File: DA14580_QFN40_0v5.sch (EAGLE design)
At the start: 29 parts, among them CON1 CON_TC2030-CTL-NL, IC1 IC_MEMORY_8P_AT25XE011_SOP, IC2 NC7SZ00M5XCT-ND, IC3 LDO5_3.3_SOT23, Q1 728-1076-1-ND, Q2 16M_2520, U1 DA14583AT2, X1 SSW-114-02-S-S, X2 SSW-114-02-S-S

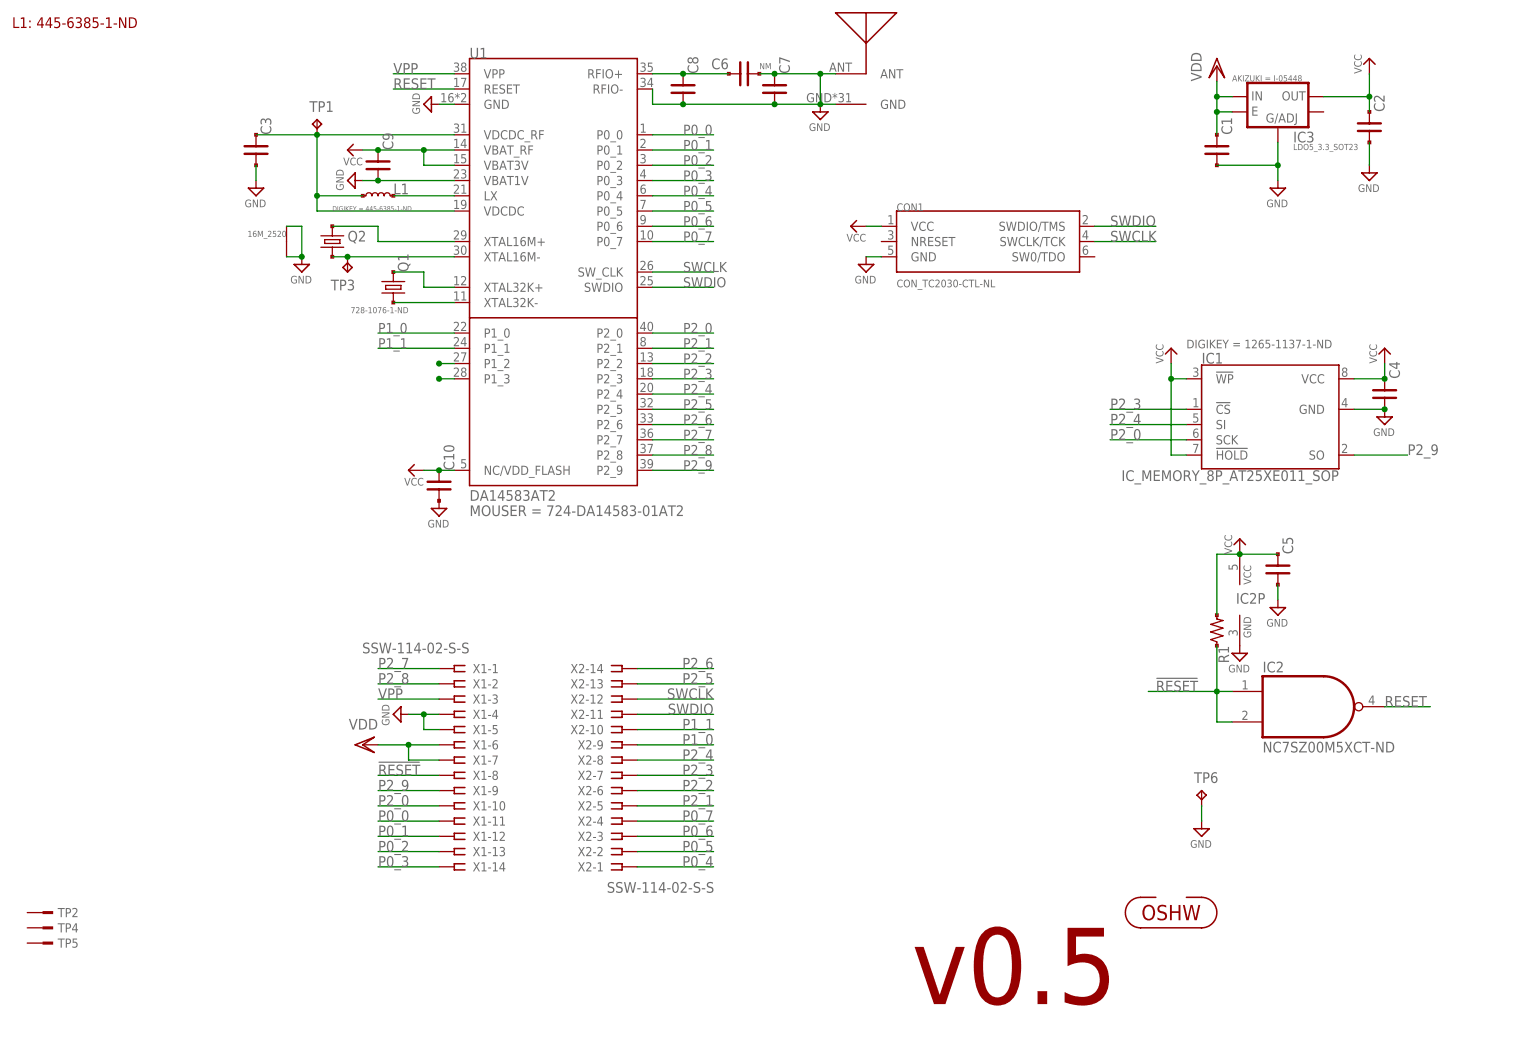
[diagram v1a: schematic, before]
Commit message: [ 58x ] IC1 - tCream; add a selecter (580 or 583)
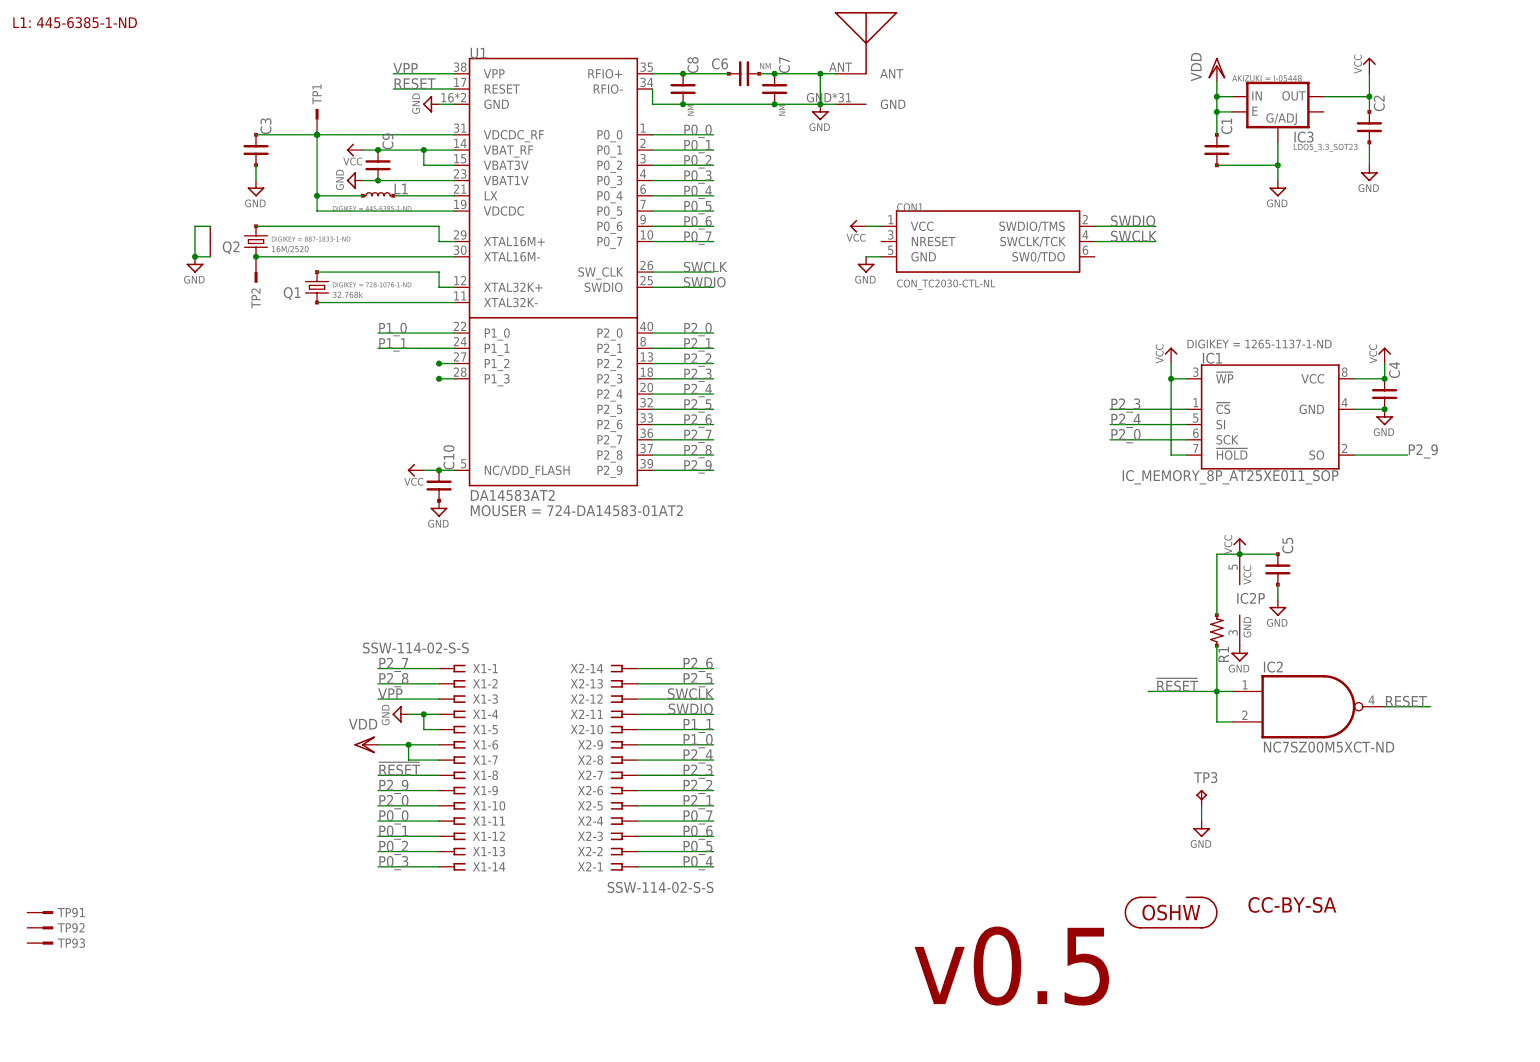
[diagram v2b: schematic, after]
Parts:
- removed TP6: TPPAD1-13, testpad_local:TPPAD1-13
- added TP91: TESTPAD_F, mylib:TESTPAD_F
- C7, C8: value (none) -> NM
- Q1: value 728-1076-1-ND -> 32.768k
- Q2: value 16M_2520 -> 16M/2520
- TP1: value TPTP07R -> TESTPAD; device testpad_local:TPTP07R -> mylib:TESTPAD
- TP2: value TESTPAD_F -> TESTPAD; device mylib:TESTPAD_F -> mylib:TESTPAD
- TP3: value TPTP07R -> TPPAD1-13; device testpad_local:TPTP07R -> testpad_local:TPPAD1-13
- renumbered TP4 to TP92, TP5 to TP93
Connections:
- net GND: now also TP3.TP; no longer TP6.TP
- net N$21: now also TP2.1; no longer TP3.TP
- net N$9: now also TP1.1; no longer TP1.TP
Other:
- note added: "CC-BY-SA"
- moved on the sheet: Q1, Q2, TP2, TP3
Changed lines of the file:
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@@
 <part name="VDD1" library="supply1" deviceset="VDD" device=""/>
 <part name="P+1" library="mylib" deviceset="VCC" device=""/>
-<part name="Q1" library="mylib" deviceset="CRYSTAL2_*" device="_FC-135" technology="32.768K" value="728-1076-1-ND"/>
+<part name="Q1" library="mylib" deviceset="CRYSTAL2_*" device="_FC-135" technology="32.768K" value="32.768k"/>
 <part name="SUPPLY7" library="mylib" deviceset="GND" device=""/>
 <part name="SUPPLY8" library="mylib" deviceset="GND" device=""/>
@@
 <part name="C4" library="mylib" deviceset="C_SMD_*" device="_1005" technology="0.1U"/>
 <part name="SUPPLY13" library="mylib" deviceset="GND" device=""/>
-<part name="TP1" library="testpad_local" deviceset="TP" device="TP07R" value="TPTP07R"/>
 <part name="X1" library="con-samtec.local" deviceset="SSW-114-02-S-S" device=""/>
 <part name="X2" library="con-samtec.local" deviceset="SSW-114-02-S-S" device=""/>
@@
 <part name="SUPPLY12" library="mylib" deviceset="GND" device=""/>
 <part name="P+4" library="mylib" deviceset="VCC" device=""/>
-<part name="TP3" library="testpad_local" deviceset="TP" device="TP07R" value="TPTP07R"/>
 <part name="P+5" library="mylib" deviceset="VCC" device=""/>
 <part name="IC3" library="mylib" deviceset="LDO5_*" device="_SOT23" technology="3.3" value="LDO5_3.3_SOT23"/>
 <part name="IC2" library="74xx-little-us_local" deviceset="74*1G00" device="DBV" technology="LVC" value="NC7SZ00M5XCT-ND"/>
-<part name="TP6" library="testpad_local" deviceset="TP" device="PAD1-13"/>
+<part name="TP3" library="testpad_local" deviceset="TP" device="PAD1-13"/>
 <part name="C6" library="mylib" deviceset="C_SMD_*" device="_1005" technology="10P" value="NM"/>
-<part name="C7" library="mylib" deviceset="C_SMD_*" device="_1005"/>
-<part name="C8" library="mylib" deviceset="C_SMD_*" device="_1005"/>
+<part name="C7" library="mylib" deviceset="C_SMD_*" device="_1005" value="NM"/>
+<part name="C8" library="mylib" deviceset="C_SMD_*" device="_1005" value="NM"/>
 <part name="C9" library="mylib" deviceset="C_SMD_*" device="_1005" technology="1.0U"/>
 <part name="C10" library="mylib" deviceset="C_SMD_*" device="_1005" technology="0.1U"/>
@@
 <part name="U$2" library="mylib" deviceset="ICON_OSHW" device=""/>
 <part name="P+6" library="mylib" deviceset="VCC" device=""/>
-<part name="Q2" library="mylib" deviceset="CRYSTAL4_*" device="_2520" technology="16M" value="16M_2520"/>
+<part name="Q2" library="mylib" deviceset="CRYSTAL4_*" device="_2520" technology="16M" value="16M/2520"/>
 <part name="P+7" library="mylib" deviceset="VCC" device=""/>
-<part name="TP2" library="mylib" deviceset="TESTPAD" device="_F"/>
-<part name="TP4" library="mylib" deviceset="TESTPAD" device="_F"/>
-<part name="TP5" library="mylib" deviceset="TESTPAD" device="_F"/>
+<part name="TP91" library="mylib" deviceset="TESTPAD" device="_F"/>
+<part name="TP92" library="mylib" deviceset="TESTPAD" device="_F"/>
+<part name="TP93" library="mylib" deviceset="TESTPAD" device="_F"/>
+<part name="TP1" library="mylib" deviceset="TESTPAD" device=""/>
+<part name="TP2" library="mylib" deviceset="TESTPAD" device=""/>
 </parts>
 <sheets>
@@
 <text x="162.56" y="5.08" size="12.7" layer="94">v0.5</text>
 <text x="12.7" y="167.64" size="1.778" layer="94">L1: 445-6385-1-ND</text>
+<text x="218.44" y="20.32" size="2.54" layer="94">CC-BY-SA</text>
 </plain>
 <instances>
@@
 <instance part="VDD1" gate="G$1" x="213.36" y="161.29"/>
 <instance part="P+1" gate="VCC" x="238.76" y="162.56"/>
-<instance part="Q1" gate="G$1" x="76.2" y="124.46" smashed="yes">
-<attribute name="NAME" x="78.74" y="127" size="1.778" layer="95" rot="R90"/>
-<attribute name="VALUE" x="78.74" y="121.158" size="1.016" layer="96" rot="R180"/>
+<instance part="Q1" gate="G$1" x="63.5" y="124.46" smashed="yes">
+<attribute name="NAME" x="60.96" y="124.46" size="1.778" layer="95" rot="R180"/>
+<attribute name="VALUE" x="66.04" y="122.682" size="1.016" layer="96"/>
+<attribute name="DIGIKEY" x="66.04" y="124.46" size="0.8128" layer="96" display="both"/>
 </instance>
-<instance part="SUPPLY7" gate="GND" x="60.96" y="127"/>
+<instance part="SUPPLY7" gate="GND" x="43.18" y="127"/>
 <instance part="SUPPLY8" gate="GND" x="223.52" y="139.7"/>
 <instance part="P+2" gate="VCC" x="68.58" y="147.32" rot="R90"/>
@@
 <instance part="C4" gate="G$1" x="241.3" y="106.68"/>
 <instance part="SUPPLY13" gate="GND" x="241.3" y="101.6"/>
-<instance part="TP1" gate="G$1" x="63.5" y="152.4" smashed="yes">
-<attribute name="NAME" x="62.23" y="153.67" size="1.778" layer="95"/>
-</instance>
 <instance part="X1" gate="-1" x="86.36" y="60.96" rot="MR0"/>
 <instance part="X1" gate="-2" x="86.36" y="58.42" rot="MR0"/>
@@
 <instance part="SUPPLY12" gate="GND" x="223.52" y="69.85"/>
 <instance part="P+4" gate="VCC" x="217.17" y="82.55"/>
-<instance part="TP3" gate="G$1" x="68.58" y="127" smashed="yes" rot="R180">
-<attribute name="NAME" x="69.85" y="125.73" size="1.778" layer="95" rot="R180"/>
-</instance>
 <instance part="P+5" gate="VCC" x="78.74" y="93.98" rot="R90"/>
 <instance part="IC3" gate="G$1" x="223.52" y="158.75">
@@
 <instance part="IC2" gate="A" x="228.6" y="54.61"/>
 <instance part="IC2" gate="P" x="217.17" y="72.39"/>
-<instance part="TP6" gate="G$1" x="210.82" y="40.64"/>
+<instance part="TP3" gate="G$1" x="210.82" y="40.64"/>
 <instance part="C6" gate="G$1" x="134.62" y="160.02" rot="R90"/>
 <instance part="C7" gate="G$1" x="139.7" y="157.48"/>
@@
 <instance part="U$2" gate="G$1" x="205.74" y="20.32"/>
 <instance part="P+6" gate="VCC" x="152.4" y="134.62" rot="R90"/>
-<instance part="Q2" gate="G$1" x="66.04" y="132.08" smashed="yes" rot="R270">
-<attribute name="NAME" x="68.58" y="132.08" size="1.778" layer="95"/>
-<attribute name="VALUE" x="58.42" y="133.858" size="1.016" layer="96" rot="R180"/>
+<instance part="Q2" gate="G$1" x="53.34" y="132.08" smashed="yes" rot="R270">
+<attribute name="NAME" x="50.8" y="132.08" size="1.778" layer="95" rot="R180"/>
+<attribute name="VALUE" x="55.88" y="130.302" size="1.016" layer="96"/>
+<attribute name="DIGIKEY" x="55.88" y="132.08" size="0.8128" layer="96" display="both"/>
 </instance>
 <instance part="P+7" gate="VCC" x="241.3" y="114.3"/>
-<instance part="TP2" gate="1" x="17.78" y="20.32"/>
-<instance part="TP4" gate="1" x="17.78" y="17.78"/>
-<instance part="TP5" gate="1" x="17.78" y="15.24"/>
+<instance part="TP91" gate="1" x="17.78" y="20.32"/>
+<instance part="TP92" gate="1" x="17.78" y="17.78"/>
+<instance part="TP93" gate="1" x="17.78" y="15.24"/>
+<instance part="TP1" gate="1" x="63.5" y="152.4" rot="R90"/>
+<instance part="TP2" gate="1" x="53.34" y="127" rot="R270"/>
 </instances>
 <busses>
@@
 <segment>
 <pinref part="SUPPLY4" gate="GND" pin="GND"/>
-<pinref part="TP6" gate="G$1" pin="TP"/>
+<pinref part="TP3" gate="G$1" pin="TP"/>
 <wire x1="210.82" y1="38.1" x2="210.82" y2="35.56" width="0.1524" layer="91"/>
 </segment>
@@
 <segment>
 <pinref part="SUPPLY7" gate="GND" pin="GND"/>
-<wire x1="58.42" y1="129.54" x2="60.96" y2="129.54" width="0.1524" layer="91"/>
-<junction x="60.96" y="129.54"/>
-<wire x1="58.42" y1="134.62" x2="60.96" y2="134.62" width="0.1524" layer="91"/>
-<wire x1="60.96" y1="134.62" x2="60.96" y2="129.54" width="0.1524" layer="91"/>
+<wire x1="45.72" y1="129.54" x2="43.18" y2="129.54" width="0.1524" layer="91"/>
+<junction x="43.18" y="129.54"/>
+<wire x1="45.72" y1="134.62" x2="43.18" y2="134.62" width="0.1524" layer="91"/>
+<wire x1="43.18" y1="134.62" x2="43.18" y2="129.54" width="0.1524" layer="91"/>
 <pinref part="Q2" gate="G$1" pin="P$1"/>
 <pinref part="Q2" gate="G$1" pin="P$2"/>
@@
 <segment>
 <pinref part="Q1" gate="G$1" pin="1"/>
-<wire x1="76.2" y1="127" x2="81.28" y2="127" width="0.1524" layer="91"/>
-<wire x1="81.28" y1="127" x2="81.28" y2="124.46" width="0.1524" layer="91"/>
+<wire x1="63.5" y1="127" x2="83.82" y2="127" width="0.1524" layer="91"/>
+<wire x1="83.82" y1="127" x2="83.82" y2="124.46" width="0.1524" layer="91"/>
 <pinref part="U1" gate="G$1" pin="XTAL32K+"/>
-<wire x1="81.28" y1="124.46" x2="86.36" y2="124.46" width="0.1524" layer="91"/>
+<wire x1="83.82" y1="124.46" x2="86.36" y2="124.46" width="0.1524" layer="91"/>
 </segment>
 </net>
@@
 <segment>
 <pinref part="U1" gate="G$1" pin="XTAL32K-"/>
-<wire x1="86.36" y1="121.92" x2="76.2" y2="121.92" width="0.1524" layer="91"/>
+<wire x1="86.36" y1="121.92" x2="63.5" y2="121.92" width="0.1524" layer="91"/>
 <pinref part="Q1" gate="G$1" pin="2"/>
 </segment>
@@
 <segment>
 <pinref part="U1" gate="G$1" pin="XTAL16M+"/>
-<wire x1="86.36" y1="132.08" x2="73.66" y2="132.08" width="0.1524" layer="91"/>
-<wire x1="66.04" y1="134.62" x2="73.66" y2="134.62" width="0.1524" layer="91"/>
-<wire x1="73.66" y1="134.62" x2="73.66" y2="132.08" width="0.1524" layer="91"/>
+<wire x1="86.36" y1="132.08" x2="83.82" y2="132.08" width="0.1524" layer="91"/>
+<wire x1="53.34" y1="134.62" x2="83.82" y2="134.62" width="0.1524" layer="91"/>
+<wire x1="83.82" y1="134.62" x2="83.82" y2="132.08" width="0.1524" layer="91"/>
 <pinref part="Q2" gate="G$1" pin="1"/>
 </segment>
@@
 <segment>
 <pinref part="U1" gate="G$1" pin="XTAL16M-"/>
-<wire x1="86.36" y1="129.54" x2="68.58" y2="129.54" width="0.1524" layer="91"/>
-<pinref part="TP3" gate="G$1" pin="TP"/>
-<wire x1="68.58" y1="129.54" x2="66.04" y2="129.54" width="0.1524" layer="91"/>
-<junction x="68.58" y="129.54"/>
+<wire x1="86.36" y1="129.54" x2="53.34" y2="129.54" width="0.1524" layer="91"/>
 <pinref part="Q2" gate="G$1" pin="2"/>
+<pinref part="TP2" gate="1" pin="1"/>
+<junction x="53.34" y="129.54"/>
 </segment>
 </net>
@@
 <pinref part="C3" gate="G$1" pin="1"/>
 <pinref part="L1" gate="G$1" pin="1"/>
-<pinref part="TP1" gate="G$1" pin="TP"/>
 <junction x="63.5" y="139.7"/>
-</segment>
-</net>
+<pinref part="TP1" gate="1" pin="1"/>
+<junction x="63.5" y="149.86"/>
+</segment>
+</net>

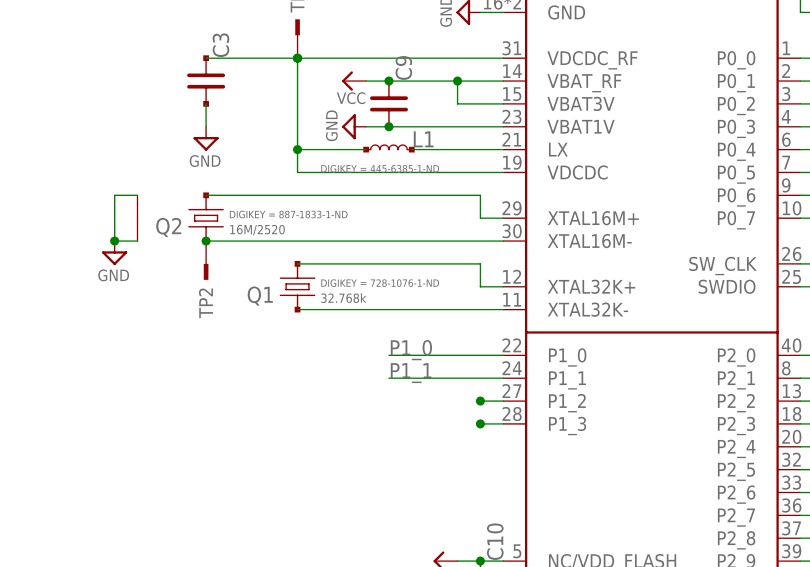
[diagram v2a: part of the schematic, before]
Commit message: [ 58x ] Q1 Digikey number replace
728-1076-1-ND  -> 1253-1342-1-ND
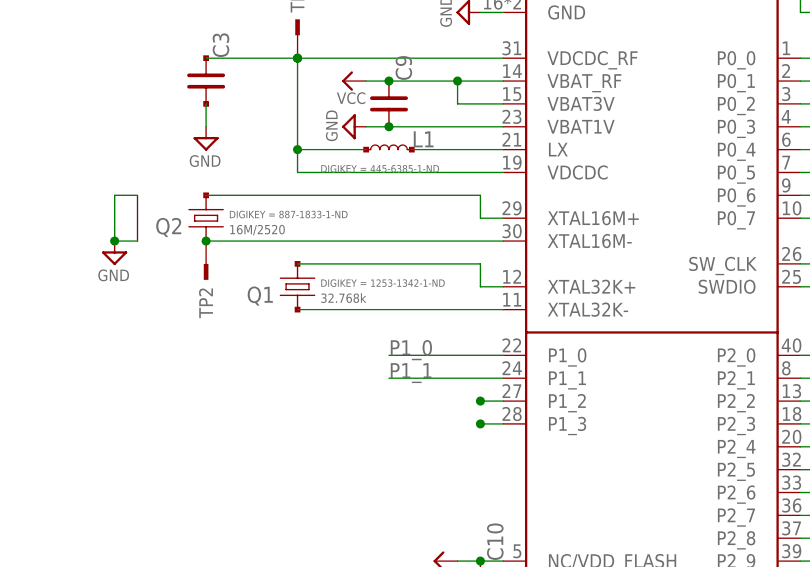
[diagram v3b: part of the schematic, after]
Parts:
- L1: value INDUCTOR_2.2U_1608 -> (none)
- TP1, TP2: value TESTPAD -> (none)
- TP91, TP92, TP93: value TESTPAD_F -> (none)
- U$2: value ICON_OSHW -> (none)
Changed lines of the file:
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@@
 <part name="SUPPLY11" library="mylib" deviceset="GND" device=""/>
 <part name="C3" library="mylib" deviceset="C_SMD_*" device="_1005" technology="1.0U"/>
-<part name="L1" library="mylib" deviceset="INDUCTOR_" device="_1608" technology="2.2U" value=""/>
+<part name="L1" library="mylib" deviceset="INDUCTOR_" device="_1608" technology="2.2U"/>
 <part name="R1" library="mylib" deviceset="R_US_*" device="_1005" technology="10K"/>
 <part name="IC1" library="mylib" deviceset="IC_MEMORY_8P_*" device="_SOP" technology="AT25XE011" value="IC_MEMORY_8P_AT25XE011_SOP"/>
